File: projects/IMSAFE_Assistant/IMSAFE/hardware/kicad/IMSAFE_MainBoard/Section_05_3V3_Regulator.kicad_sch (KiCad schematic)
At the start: 8 parts, among them U7 TPS62133RGTR

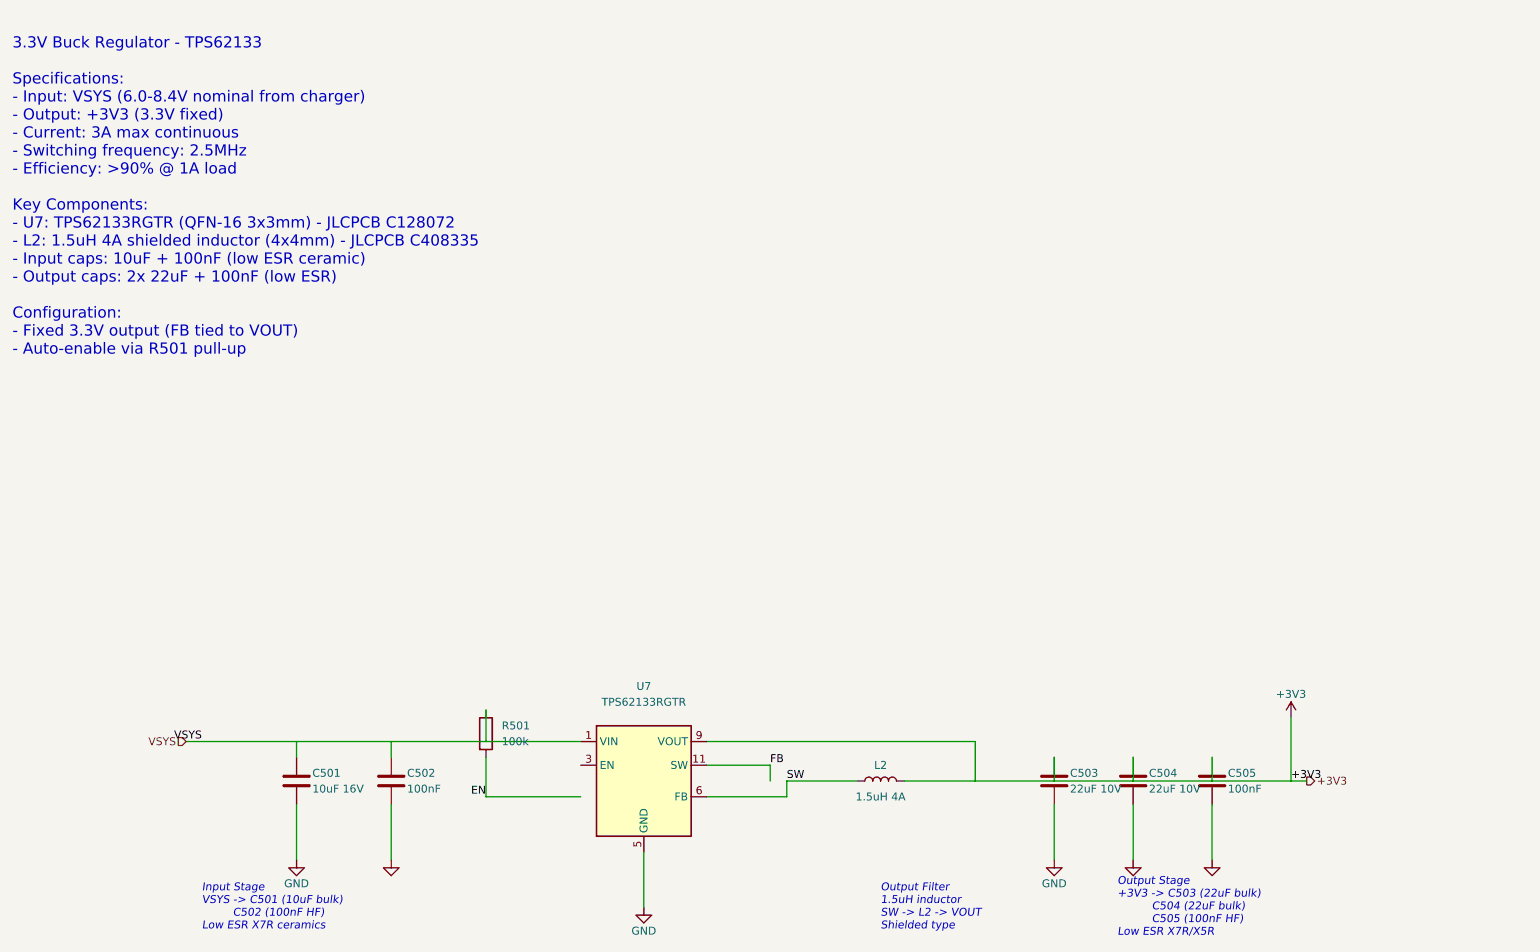
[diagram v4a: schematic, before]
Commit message: Update KiCad schematics and add analysis files
- Update all MainBoard schematic sections with component placement
- Add ERC reports and analysis scripts for schematic validation
- Update Radar Interface and SwitchLED Board projects
- Sync KiCad project files with latest session changes

Co-Authored-By: Claude Opus 4.5 <noreply@anthropic.com>
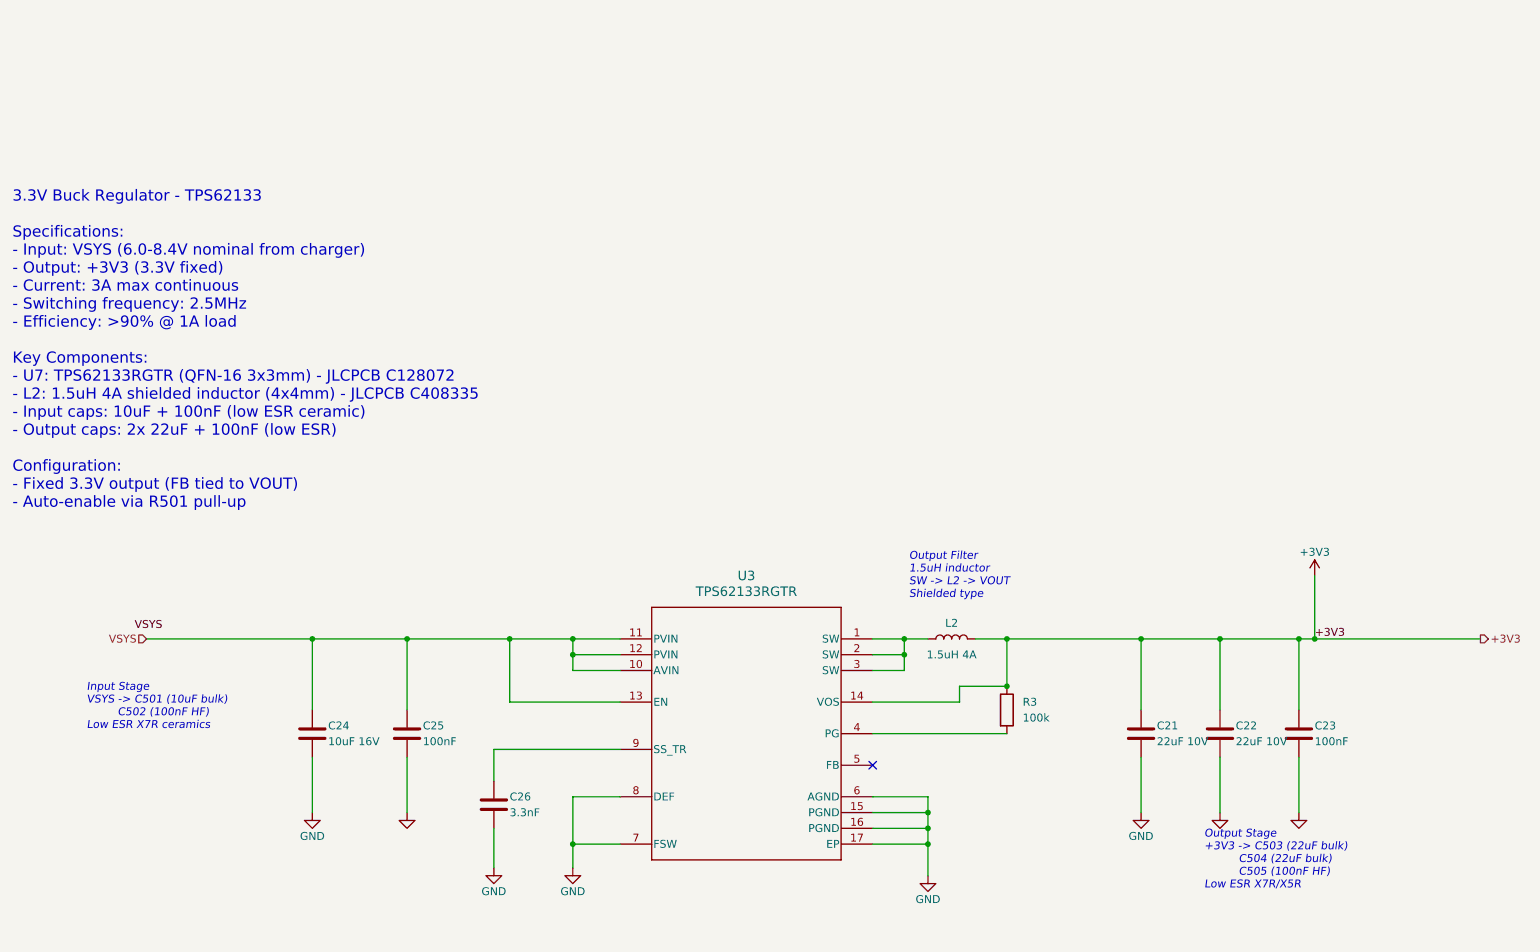
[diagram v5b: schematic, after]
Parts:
- removed C501: 10uF 16V, Capacitor_SMD:C_0805_2012Metric, symbol Device:C
- removed C502, C505: 100nF, Capacitor_SMD:C_0603_1608Metric, symbol Device:C
- removed C503, C504: 22uF 10V, Capacitor_SMD:C_0805_2012Metric, symbol Device:C
- removed R501: 100k, Resistor_SMD:R_0603_1608Metric, symbol Device:R
- removed U7: TPS62133RGTR, Package_DFN_QFN:QFN-16-1EP_3x3mm_P0.5mm_EP1.8x1.8mm, symbol Regulator:TPS62133RGTR
- added C21, C22: 22uF 10V, Capacitor_SMD:C_0805_2012Metric, symbol Device:C
- added C23, C25: 100nF, Capacitor_SMD:C_0603_1608Metric, symbol Device:C
- added C24: 10uF 16V, Capacitor_SMD:C_0805_2012Metric, symbol Device:C
- added C26: 3.3nF, Capacitor_SMD:C_0603_1608Metric, symbol Device:C
- added R3: 100k, Resistor_SMD:R_0603_1608Metric, symbol Device:R
- added U3: TPS62133RGTR, RGT0016C, symbol 1_New_library:TPS62133RGTR
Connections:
- net +3V3: now also C21.1, C22.1, C23.1, R3.1, U3.14 (VOS)
- net GND: now also C21.2, C22.2, C23.2, C24.2, C25.2, C26.2, U3.15 (PGND), U3.16 (PGND), U3.17 (EP), U3.6 (AGND), U3.7 (FSW), U3.8 (DEF)
- net VSYS: now also C24.1, C25.1, U3.10 (AVIN), U3.11 (PVIN), U3.12 (PVIN), U3.13 (EN)
- net SW: no longer names the net of L2.1
- net SW: now also U3.1 (SW), U3.2 (SW), U3.3 (SW)
- new net: R3.2, U3.4 (PG)
- new net: C26.1, U3.9 (SS_TR)
- no-connect marks 0 -> 1
